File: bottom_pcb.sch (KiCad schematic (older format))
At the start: 14 parts

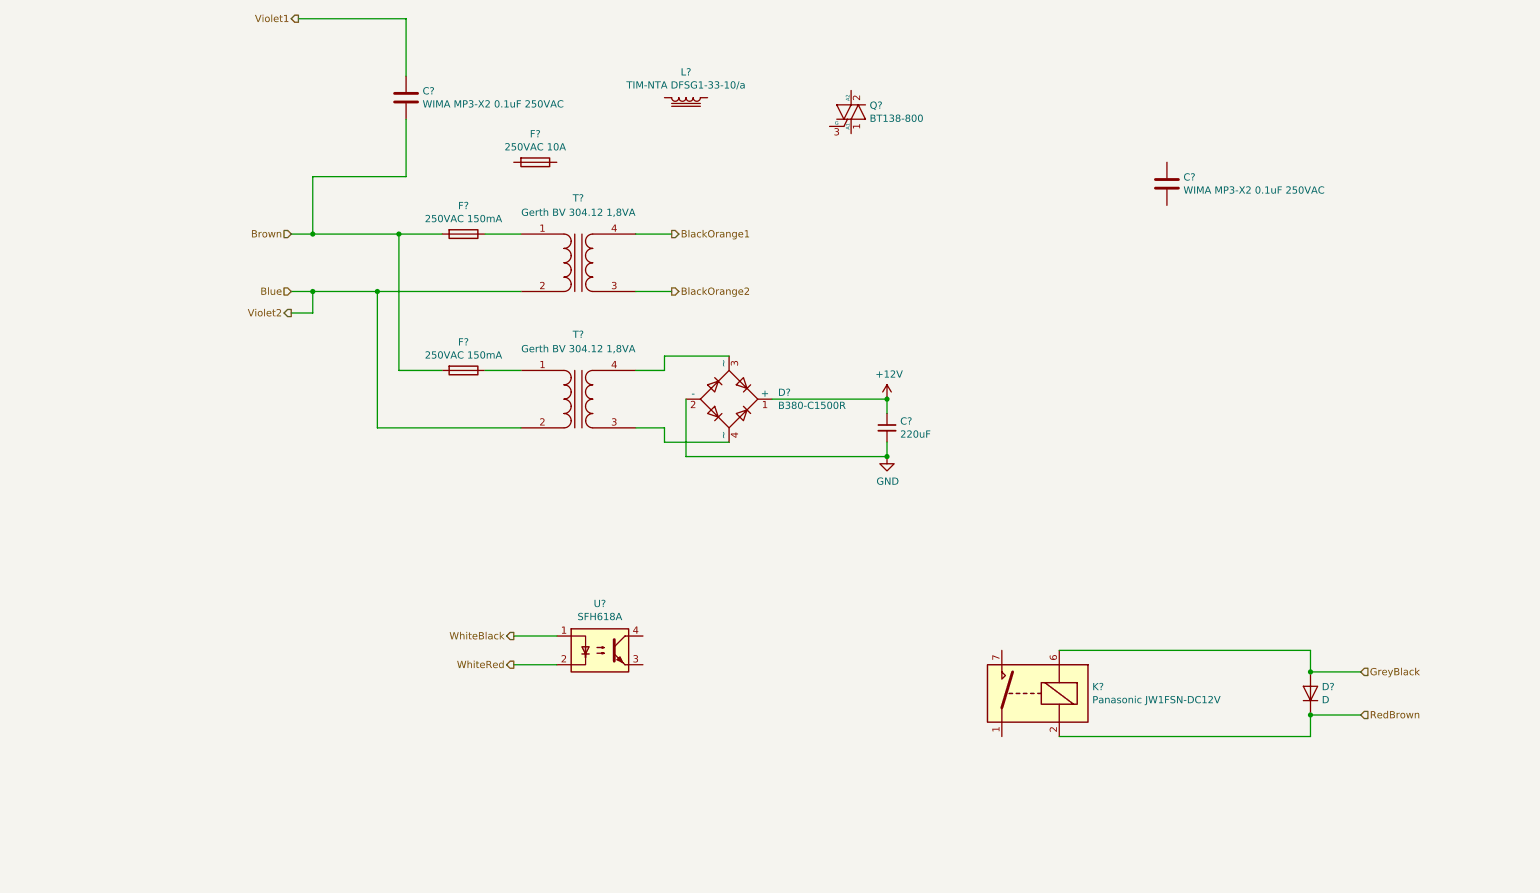
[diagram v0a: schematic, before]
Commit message: Bottom PCB schematic is functionally complete
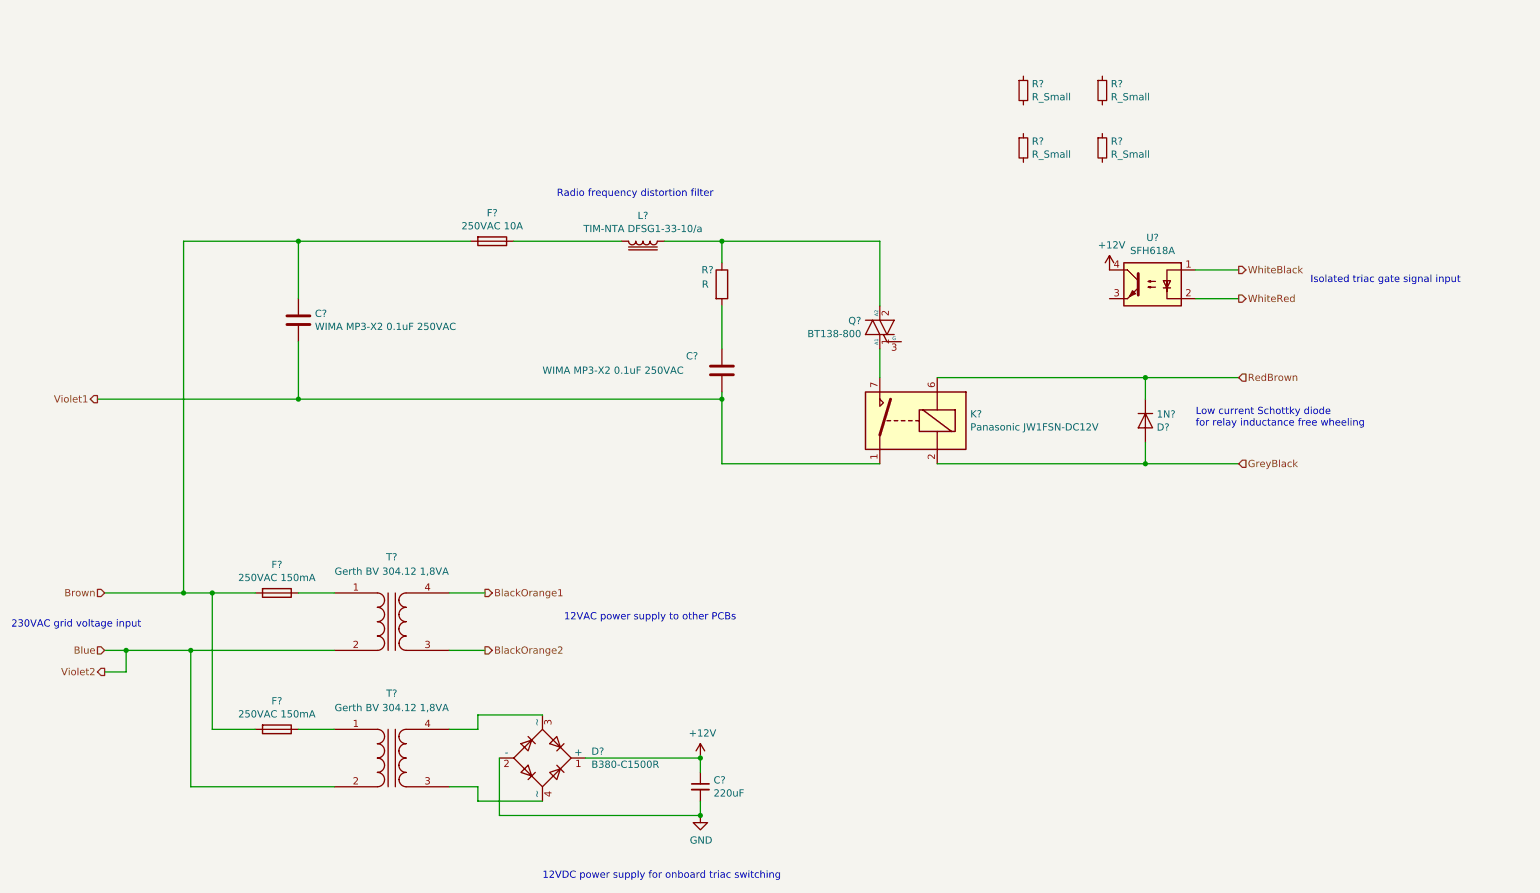
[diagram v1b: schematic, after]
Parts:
- added R?: R, symbol Device:R
- added R? (x4): R_Small, symbol Device:R_Small
- D?: value D -> 1N?
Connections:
- net +12V: now also U?.4
- net Brown: now also C?.1, F?.2; no longer C?.2
- net GreyBlack: now also K?.2; no longer K?.6
- net RedBrown: now also K?.6; no longer K?.2
- net Violet1: now also C?.2, C?.2, K?.1, K?.14; no longer C?.1
- net at L?.1: now also Q?.2 (A2), R?.1
- net at L?.2: now also F?.1
- net at C?.1: now also R?.2
- net at K?.7, K?.8: now also Q?.1 (A1)
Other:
- note added: "12VAC power supply to other PCBs"
- note added: "12VDC power supply for onboard triac switching"
- note added: "230VAC grid voltage input"
- note added: "Isolated triac gate signal input"
- note added: "Low current Schottky diode\nfor relay inductance free wheeling"
- note added: "Radio frequency distortion filter"
- moved on the sheet: C?, D?, F?, K?, L?, Q?, T?, U?

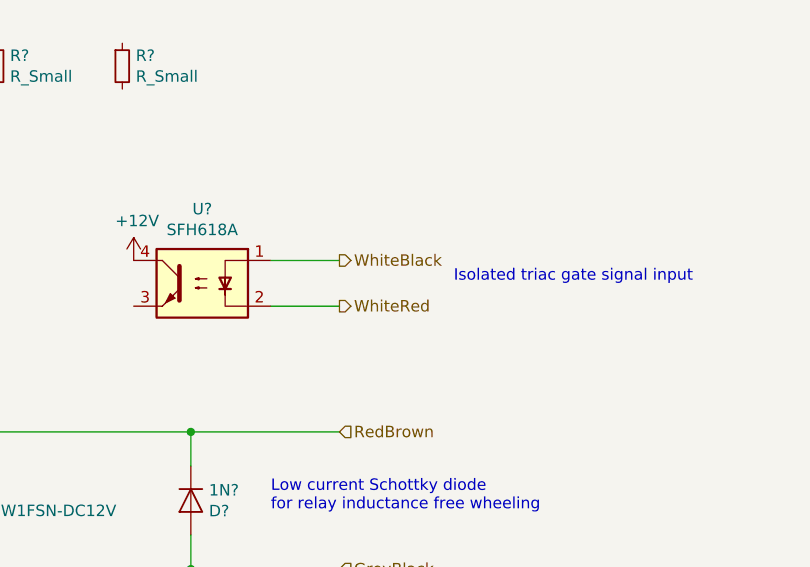
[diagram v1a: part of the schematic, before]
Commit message: Added D-Sub 9 connector
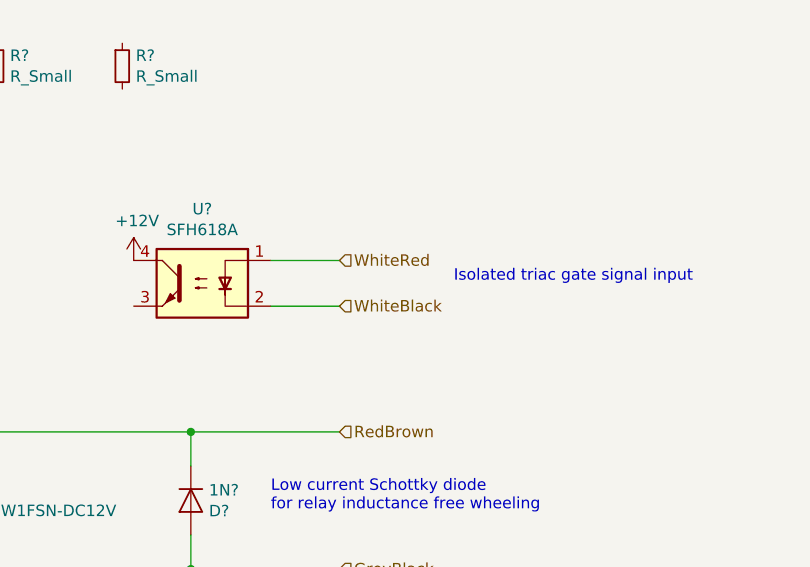
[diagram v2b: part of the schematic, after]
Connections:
- net WhiteBlack: now also U?.2; no longer U?.1
- net WhiteRed: now also U?.1; no longer U?.2
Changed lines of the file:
@@
 Wire Wire Line
 	8650 4100 8650 3950
-Text HLabel 9300 2750 2    50   Output ~ 0
+Text HLabel 9300 2950 2    50   Input ~ 0
 WhiteBlack
-Text HLabel 9300 2950 2    50   Output ~ 0
+Text HLabel 9300 2750 2    50   Input ~ 0
 WhiteRed
 Text HLabel 4050 5000 2    50   Output ~ 0
